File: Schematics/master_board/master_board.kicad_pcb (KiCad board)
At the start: 2 copper layers, 156 x 156 mm, 74 parts, among them J1 2x5x1.27mm, J2 USB_C_Receptacle_USB2.0, J3 Conn_01x01_Female, J4 Conn_01x01_Female, J5 Conn_01x01_Female, J6 Conn_01x01_Female, M0 Conn_01x06_Male, M1 Conn_01x06_Male, M10 Conn_01x06_Male, M11 Conn_01x06_Male, M12 Conn_01x06_Male, M13 Conn_01x06_Male, M14 Conn_01x06_Male, M15 Conn_01x06_Male, M16 Conn_01x06_Male, M17 Conn_01x06_Male, M18 Conn_01x06_Male, M19 Conn_01x06_Male, M2 Conn_01x06_Male, M3 Conn_01x06_Male, M4 Conn_01x06_Male, M5 Conn_01x06_Male, M6 Conn_01x06_Male, M7 Conn_01x06_Male, M8 Conn_01x06_Male, M9 Conn_01x06_Male, SW1 SW_Push, SW2 SW_Push, SW3 SW_Push, U1 NCP1117-3.3_SOT223, U2 RP2040, U3 W25Q16JVSSIQ, U4 74HCT154PW,118, U5 74HCT154PW,118, Y1 ABLS-12.000MHZ-B4-T

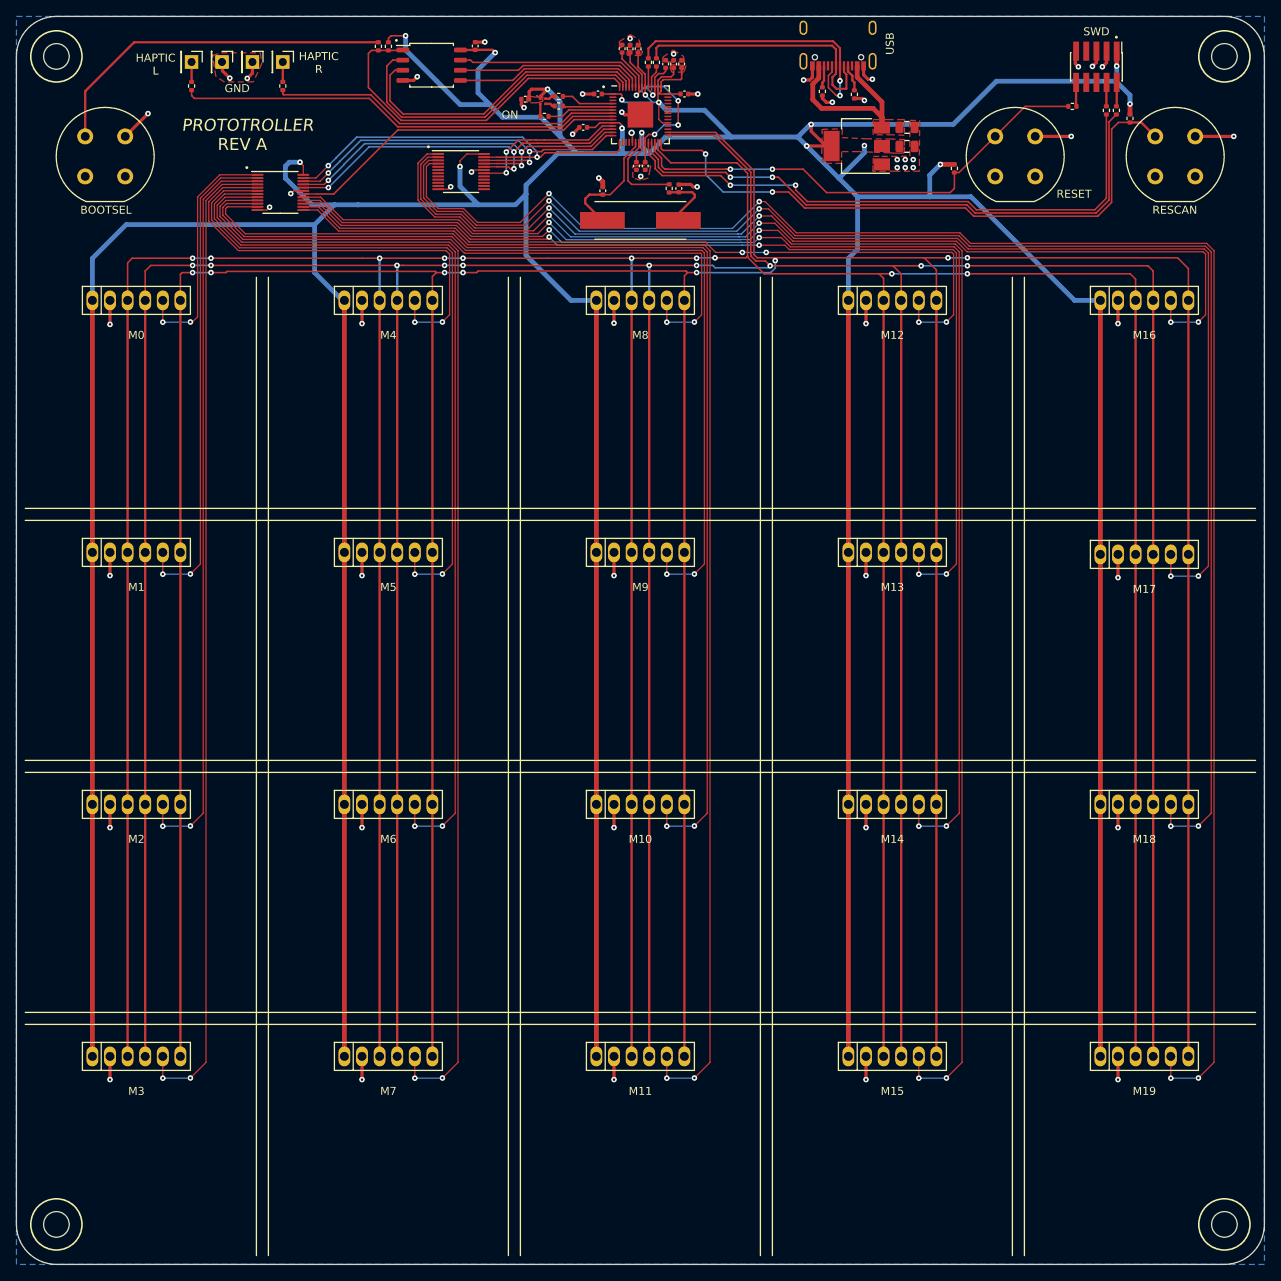
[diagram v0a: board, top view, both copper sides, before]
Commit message: Changed 10k res values to 1k, SWD pins, Decoder footprints, and haptic pins
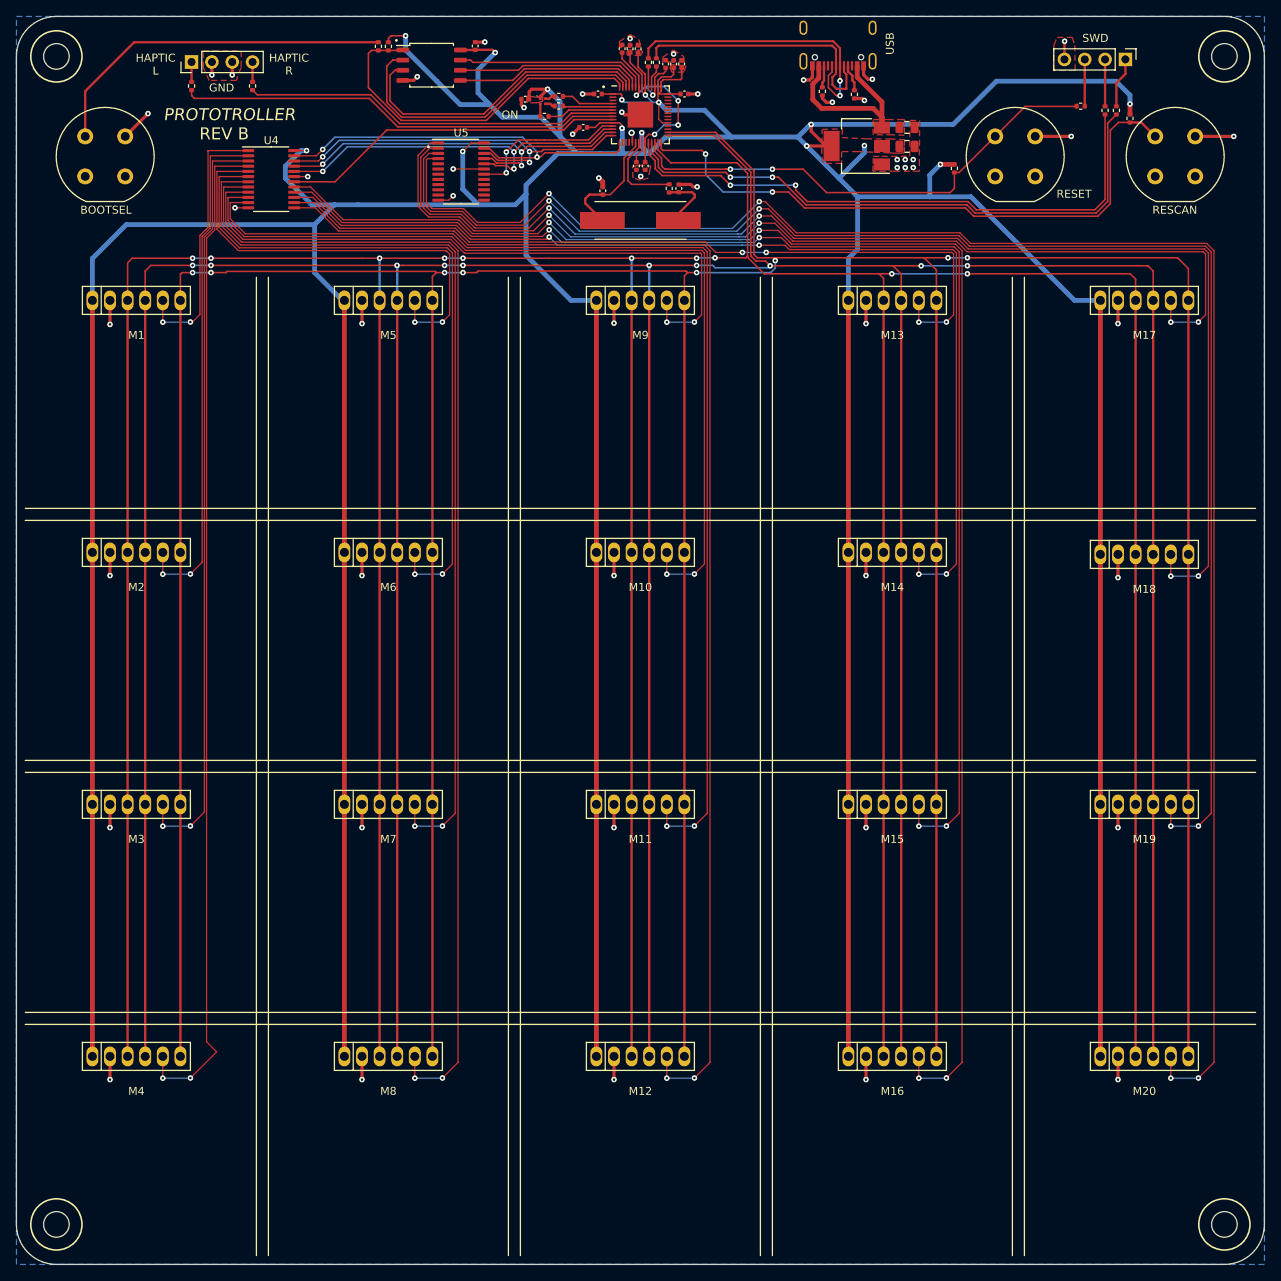
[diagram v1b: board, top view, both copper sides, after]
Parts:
- removed the J1 at (152.0, 24.3)
- removed J4, J5, J6: Conn_01x01_Female, Connector_PinHeader_2.54mm:PinHeader_1x01_P2.54mm_Vertical
- added J2: Conn_01x04_Male, Connector_PinHeader_2.54mm:PinHeader_1x04_P2.54mm_Vertical, F.Cu at (155.6, 23.4)
- J3: value Conn_01x01_Female -> Conn_01x04_Female; footprint Connector_PinHeader_2.54mm:PinHeader_1x01_P2.54mm_Vertical -> Connector_PinHeader_2.54mm:PinHeader_1x04_P2.54mm_Vertical
- R12, R13, R9: value 10k -> 1k
- R15: value 10k -> DNF
- U4, U5: footprint Package_SO:TSSOP-24_4.4x5mm_P0.4mm -> Package_SO:TSSOP-24_4.4x7.8mm_P0.65mm
- moved R17 3.78 mm to (46.5, 26.7)
- moved U4 2.01 mm to (48.9, 38.4)
- moved R6 1.04 mm to (150.0, 29.2)
- moved R5 0.16 mm to (153.1, 29.8)
- turned J3 to 90 degrees
- renumbered J2 to J1, M0 to M1, M9 to M10, M10 to M11, M11 to M12, M12 to M13, M13 to M14, M14 to M15, M15 to M16, M16 to M17, M17 to M18, M18 to M19, M1 to M2, M19 to M20, M2 to M3, M3 to M4, M4 to M5, M5 to M6, M6 to M7, M7 to M8, M8 to M9
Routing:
- net /HAP_R: track 43.8 -> 47.3 mm
- net /CONN_SWDIO: track 3.01 -> 6.33 mm
- net GND: track 113.3 -> 110.1 mm, vias 55 -> 53
- net /CONN_SWCLK: track 3.00 -> 5.86 mm
- net /CONN_RUN_N: track 3.02 -> 5.85 mm
- net /5-to-32/SPI_CSN0: track 31.0 -> 33.8 mm
- net /5-to-32/SPI_CSN3: track 123.9 -> 126.6 mm
- net /5-to-32/SPI_CSN1: track 61.8 -> 64.2 mm
- net /5-to-32/SPI_CSN2: track 92.9 -> 94.9 mm
- net +3V3: track 877.0 -> 875.2 mm, vias 16 -> 15
- net /5-to-32/SPI_CSN15: track 197.6 -> 199.3 mm
- net /5-to-32/SPI_CSN16: track 126.9 -> 128.5 mm
- net /5-to-32/SPI_CSN14: track 164.4 -> 166.0 mm
- net /5-to-32/SPI_CSN13: track 131.2 -> 132.7 mm
- net /5-to-32/SPI_CSN17: track 159.1 -> 160.5 mm
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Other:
- board text added: "REV B"
- board text removed: "REV A"
- board text removed: "Yu-yang Hsieh (Leo) Caleb O'Malley Britton McLeavy Merrick Ryman Evan Zhang Made with <3"

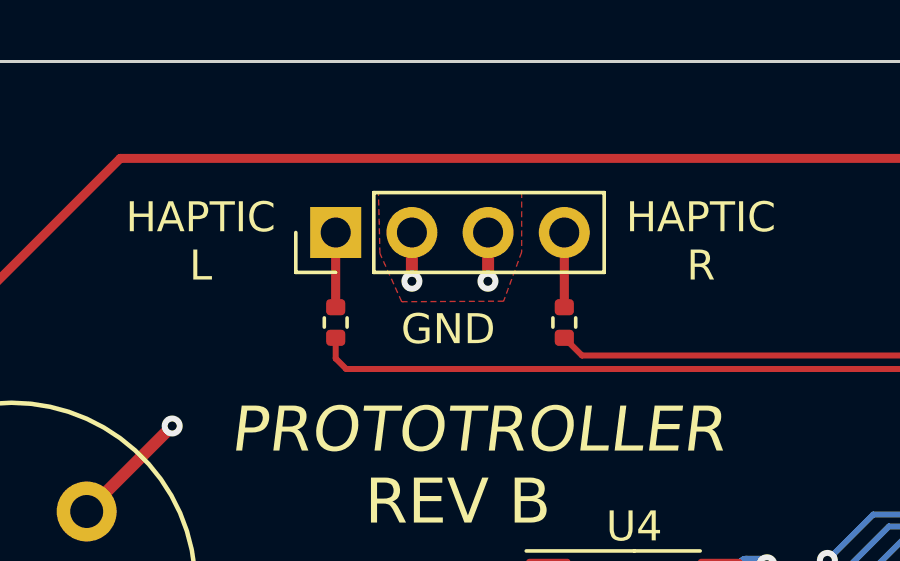
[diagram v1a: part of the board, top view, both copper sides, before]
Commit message: Minor alignment with male 1-4 pins
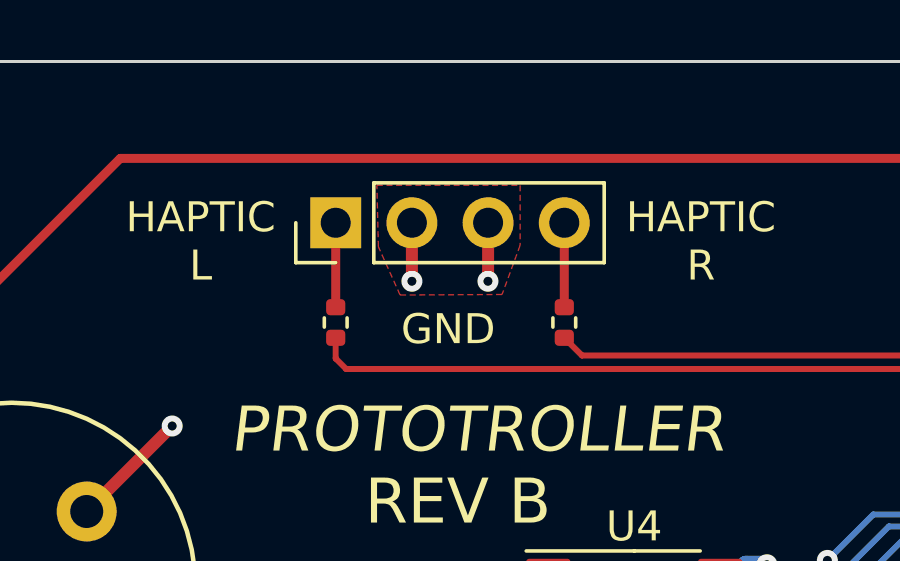
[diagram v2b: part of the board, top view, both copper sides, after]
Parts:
- moved J3 0.32 mm to (38.9, 23.4)
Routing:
- net GND: track 110.1 -> 110.8 mm
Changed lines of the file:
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@@
   )
   (footprint "Connector_PinHeader_2.54mm:PinHeader_1x04_P2.54mm_Vertical" (layer "F.Cu")
-    (at 38.9 23.7 90)
+    (at 38.9 23.375 90)
     (descr "Through hole straight pin header, 1x04, 2.54mm pitch, single row")
     (tags "Through hole pin header THT 1x04 2.54mm single row")
@@
   (segment (start 117.75 27.885) (end 117.75 28.25) (width 0.4) (layer "F.Cu") (net 2))
   (segment (start 100.98 27.7) (end 102.175 27.7) (width 0.4) (layer "F.Cu") (net 2))
+  (segment (start 41.44 25.325) (end 41.44 23.375) (width 0.4) (layer "F.Cu") (net 2))
   (segment (start 91.7 53.5) (end 91.7 56.35) (width 0.4) (layer "F.Cu") (net 2))
   (segment (start 122.9 24.18) (end 122.9 25.3) (width 0.4) (layer "F.Cu") (net 2))
   (segment (start 89.8 38.2) (end 90.3 38.7) (width 0.6) (layer "F.Cu") (net 2))
-  (segment (start 43.975 25.325) (end 43.98 25.32) (width 0.4) (layer "F.Cu") (net 2))
   (segment (start 74.35 21.22) (end 75.53 21.22) (width 0.4) (layer "F.Cu") (net 2))
   (segment (start 116.163288 25.95) (end 115.4 25.95) (width 0.4) (layer "F.Cu") (net 2))
@@
   (segment (start 60.2 148) (end 60.2 150.9) (width 0.4) (layer "F.Cu") (net 2))
   (segment (start 28.7 53.5) (end 28.7 56.5) (width 0.4) (layer "F.Cu") (net 2))
+  (segment (start 43.975 25.325) (end 43.98 25.32) (width 0.4) (layer "F.Cu") (net 2))
   (segment (start 80.12 28.35) (end 80.12 29.07) (width 0.4) (layer "F.Cu") (net 2))
   (segment (start 122.76 28.26) (end 123 28.5) (width 0.4) (layer "F.Cu") (net 2))
-  (segment (start 43.98 25.32) (end 43.98 23.7) (width 0.4) (layer "F.Cu") (net 2))
   (segment (start 101.3 39) (end 99.82 39) (width 0.4) (layer "F.Cu") (net 2))
   (segment (start 116.5 24.18) (end 116.5 25.613288) (width 0.4) (layer "F.Cu") (net 2))
@@
   (segment (start 123.2 85) (end 123.2 87.9) (width 0.4) (layer "F.Cu") (net 2))
   (segment (start 148.005 21.12) (end 148.005 23.375) (width 0.3) (layer "F.Cu") (net 2))
-  (segment (start 41.44 25.325) (end 41.44 23.7) (width 0.4) (layer "F.Cu") (net 2))
   (segment (start 28.7 116.5) (end 28.7 119.4) (width 0.4) (layer "F.Cu") (net 2))
+  (segment (start 43.98 25.32) (end 43.98 23.375) (width 0.4) (layer "F.Cu") (net 2))
   (segment (start 86.525 32.725) (end 86.525 32.72) (width 0.4) (layer "F.Cu") (net 2))
   (segment (start 164.35 33) (end 169.175 33) (width 0.4) (layer "F.Cu") (net 2))
@@
   (segment (start 117.95 24.18) (end 117.95 26.066002) (width 0.3) (layer "F.Cu") (net 17))
   (segment (start 117.75 26.266002) (end 117.75 26.865) (width 0.3) (layer "F.Cu") (net 17))
-  (segment (start 38.9 26.19) (end 38.9 23.7) (width 0.3) (layer "F.Cu") (net 19))
-  (segment (start 46.52 23.7) (end 46.52 26.19) (width 0.3) (layer "F.Cu") (net 20))
+  (segment (start 38.9 26.19) (end 38.9 23.375) (width 0.3) (layer "F.Cu") (net 19))
+  (segment (start 46.52 23.375) (end 46.52 26.19) (width 0.3) (layer "F.Cu") (net 20))
   (segment (start 38.75 56.45) (end 39.9415 55.2585) (width 0.15) (layer "F.Cu") (net 21))
   (segment (start 39.9415 55.2585) (end 39.9415 45.372023) (width 0.15) (layer "F.Cu") (net 21))
@@
     (polygon
       (pts
-        (xy 45.1 24.35)
-        (xy 44.497596 25.989718)
-        (xy 41.1 26.007721)
-        (xy 40.375 24.4)
-        (xy 40.325 22.35)
-        (xy 45.1 22.35)
+        (xy 45.047624 24.126564)
+        (xy 44.44522 25.766282)
+        (xy 41.047624 25.784285)
+        (xy 40.322624 24.176564)
+        (xy 40.272624 22.126564)
+        (xy 45.047624 22.126564)
       )
     )
